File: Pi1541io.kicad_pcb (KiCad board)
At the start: 2 copper layers, 65 x 56 mm, 56 parts, among them J1 IEC1, J10 SDA, J11 SCL, J12 I2C, J13 SDA, J14 SDA, J15 SDA, J2 IEC2, J3 IEC3, J4 ExtSpkr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

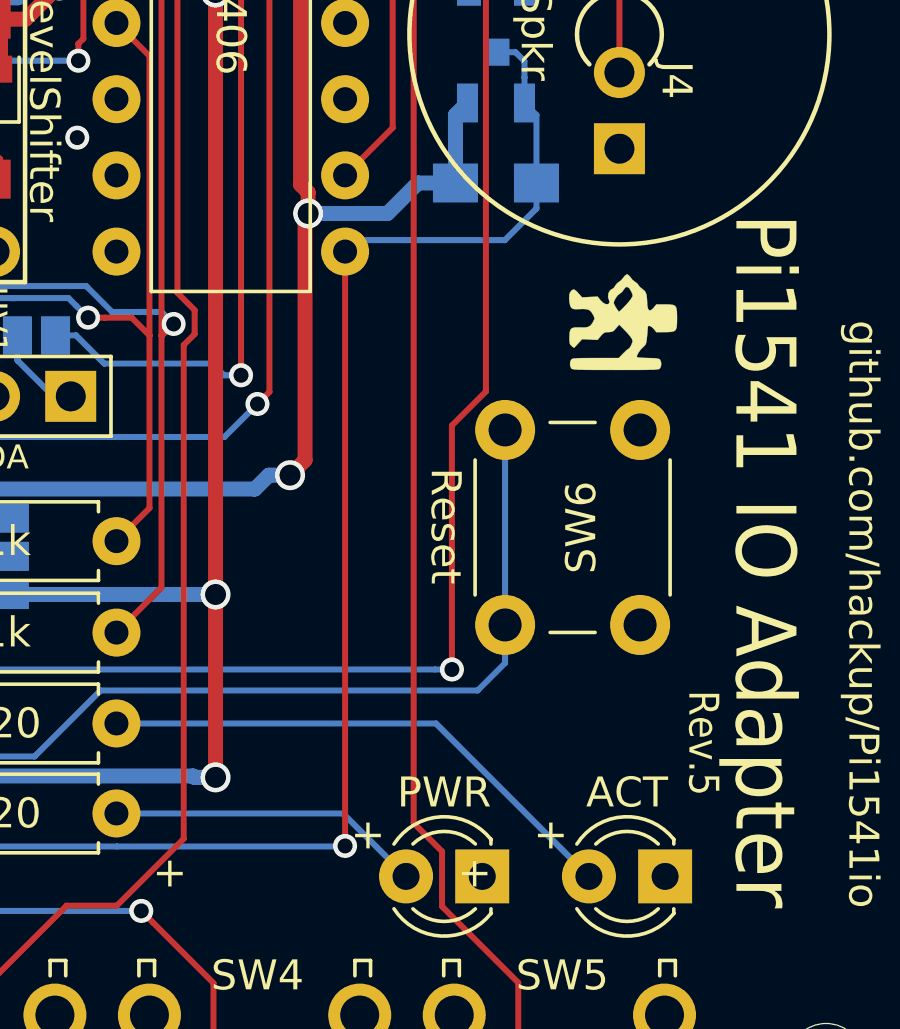
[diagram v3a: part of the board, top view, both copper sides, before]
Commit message: Added an additional solder bridge that is now needed to connect the SRQ line from the bus. This closes #1.
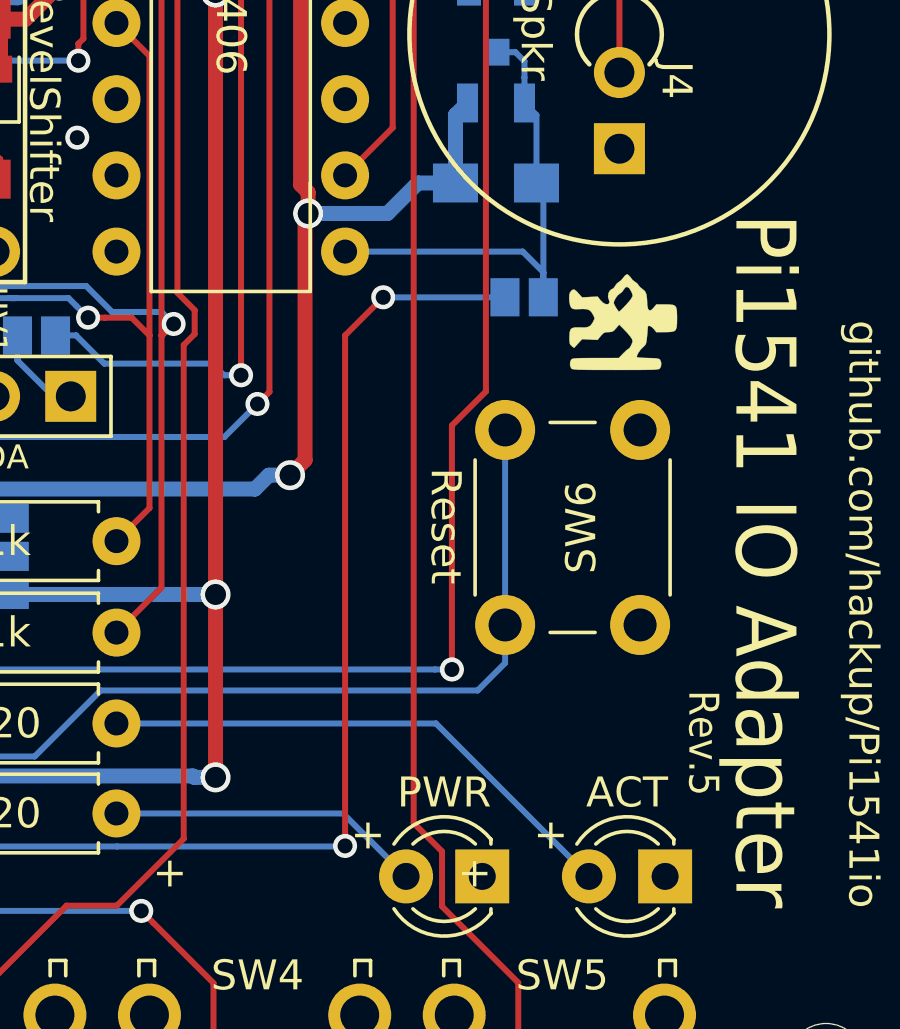
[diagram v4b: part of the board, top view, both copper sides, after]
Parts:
- added J16: GS2, Connectors:GS2, B.Cu at (157.6, 86.2)
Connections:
- Q5 pad 3: SRQ -> Net-(J16-Pad2)
- R13 pad 2: SRQ -> Net-(J16-Pad2)
- R15 pad 2: SRQ -> Net-(J16-Pad2)
- U2 pad 8: SRQ -> Net-(J16-Pad2)
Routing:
- net Net-(J16-Pad2): track 0.00 -> 16.9 mm
- net SRQ: track 89.8 -> 79.8 mm, vias 1 -> 2
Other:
- board text added: "enable"
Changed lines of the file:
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@@
   (general
     (thickness 1.6)
-    (drawings 120)
-    (tracks 610)
+    (drawings 121)
+    (tracks 613)
     (zones 0)
-    (modules 56)
-    (nets 41)
+    (modules 57)
+    (nets 42)
   )
   (page A4)
@@
   (net 39 "Net-(J12-Pad4)")
   (net 40 "Net-(J13-Pad1)")
+  (net 41 "Net-(J16-Pad2)")
   (net_class Default "This is the default net class."
     (clearance 0.2)
@@
     (add_net "Net-(J10-Pad2)")
     (add_net "Net-(J11-Pad2)")
+    (add_net "Net-(J16-Pad2)")
     (add_net "Net-(J4-Pad1)")
     (add_net RESET)
@@
       (net 20 DATA_BD))
     (pad 8 thru_hole oval (at 7.62 15.24) (size 1.6 1.6) (drill 0.8) (layers *.Cu *.Mask)
-      (net 17 SRQ))
+      (net 41 "Net-(J16-Pad2)"))
     (pad 2 thru_hole oval (at 0 2.54) (size 1.6 1.6) (drill 0.8) (layers *.Cu *.Mask)
       (net 14 DATA))
@@
       (net 30 SRQ_3V))
     (pad 3 smd rect (at 1 0 270) (size 0.9 0.8) (layers B.Cu B.Paste B.Mask)
-      (net 17 SRQ))
+      (net 41 "Net-(J16-Pad2)"))
     (model ${KISYS3DMOD}/TO_SOT_Packages_SMD.3dshapes/SOT-23.wrl
       (at (xyz 0 0 0))
@@
     )
     (pad 2 smd rect (at 0.95 0) (size 0.7 1.3) (layers B.Cu B.Paste B.Mask)
-      (net 17 SRQ))
+      (net 41 "Net-(J16-Pad2)"))
     (pad 1 smd rect (at -0.95 0) (size 0.7 1.3) (layers B.Cu B.Paste B.Mask)
       (net 2 +5V))
@@
       (net 2 +5V))
     (pad 2 smd rect (at 1.35 0) (size 1.5 1.3) (layers B.Cu B.Paste B.Mask)
-      (net 17 SRQ))
+      (net 41 "Net-(J16-Pad2)"))
     (model ${KISYS3DMOD}/Resistors_SMD.3dshapes/R_0805.wrl
       (at (xyz 0 0 0))
@@
     (pad "" np_thru_hole oval (at 0 0) (size 3.2 1.5) (drill oval 2.7 1.1) (layers *.Cu *.Mask))
   )
+  (module Connectors:GS2 (layer B.Cu)
+    (at 157.582 86.246 270)
+    (descr "2-pin solder bridge")
+    (tags "solder bridge")
+    (attr smd)
+    (fp_text reference J16 (at 0 2.54) (layer B.SilkS)
+      (effects (font (size 0.8 0.8) (thickness 0.12)) (justify mirror))
+    )
+    (fp_text value GS2 (at -1.8 0 180) (layer B.Fab)
+      (effects (font (size 1 1) (thickness 0.15)) (justify mirror))
+    )
+    (fp_line (start 1.1 1.45) (end 1.1 -1.5) (layer B.CrtYd) (width 0.05))
+    (fp_line (start 1.1 -1.5) (end -1.1 -1.5) (layer B.CrtYd) (width 0.05))
+    (fp_line (start -1.1 -1.5) (end -1.1 1.45) (layer B.CrtYd) (width 0.05))
+    (fp_line (start -1.1 1.45) (end 1.1 1.45) (layer B.CrtYd) (width 0.05))
+    (fp_line (start -0.89 1.27) (end -0.89 -1.27) (layer B.SilkS) (width 0.12))
+    (fp_line (start 0.89 -1.27) (end 0.89 1.27) (layer B.SilkS) (width 0.12))
+    (fp_line (start 0.89 -1.27) (end -0.89 -1.27) (layer B.SilkS) (width 0.12))
+    (fp_line (start -0.89 1.27) (end 0.89 1.27) (layer B.SilkS) (width 0.12))
+    (pad 1 smd rect (at 0 0.64 270) (size 1.27 0.97) (layers B.Cu B.Paste B.Mask)
+      (net 17 SRQ))
+    (pad 2 smd rect (at 0 -0.64 270) (size 1.27 0.97) (layers B.Cu B.Paste B.Mask)
+      (net 41 "Net-(J16-Pad2)"))
+  )
+  (gr_text enable (at 156.947 87.643) (layer B.SilkS)
+    (effects (font (size 0.8 0.8) (thickness 0.12)) (justify mirror))
+  )
   (gr_text + (at 158.471 104.153) (layer F.SilkS)
     (effects (font (size 1 1) (thickness 0.2)))
@@
     (effects (font (size 0.8 0.8) (thickness 0.15)))
   )
-  (gr_text "SRQ\nreserved" (at 159.487 83.706) (layer B.SilkS)
+  (gr_text "SRQ\nreserved" (at 159.487 87.262) (layer B.SilkS)
     (effects (font (size 1 1) (thickness 0.15)) (justify right mirror))
   )
-  (gr_line (start 159.487 67.958) (end 159.487 84.976) (layer B.SilkS) (width 0.1))
+  (gr_line (start 159.487 67.958) (end 159.487 88.786) (layer B.SilkS) (width 0.1))
   (gr_line (start 153.645 67.958) (end 159.487 67.958) (layer B.SilkS) (width 0.1))
-  (gr_line (start 153.645 84.976) (end 153.645 67.958) (layer B.SilkS) (width 0.1))
-  (gr_line (start 159.487 84.976) (end 153.645 84.976) (layer B.SilkS) (width 0.1))
+  (gr_line (start 153.645 88.786) (end 153.645 67.958) (layer B.SilkS) (width 0.1))
+  (gr_line (start 159.487 88.786) (end 153.645 88.786) (layer B.SilkS) (width 0.1))
   (gr_line (start 135.103 70.625) (end 135.103 70.371) (layer B.SilkS) (width 0.1))
   (gr_line (start 135.103 70.879) (end 135.103 71.133) (layer B.SilkS) (width 0.1))
@@
   (segment (start 117.577 86.228345) (end 119.127001 87.778346) (width 0.2) (layer F.Cu) (net 17))
   (segment (start 117.577 84.602) (end 117.577 86.228345) (width 0.2) (layer F.Cu) (net 17) (status 10))
-  (segment (start 157.9922 80.169) (end 157.5922 79.769) (width 0.2) (layer B.Cu) (net 17))
-  (segment (start 157.9922 82.436) (end 157.9922 80.169) (width 0.2) (layer B.Cu) (net 17))
-  (segment (start 157.5922 78.919) (end 157.5922 79.769) (width 0.2) (layer B.Cu) (net 17))
-  (segment (start 157.5922 78.3758) (end 157.5922 78.919) (width 0.2) (layer B.Cu) (net 17))
-  (segment (start 157.293 78.0766) (end 157.5922 78.3758) (width 0.2) (layer B.Cu) (net 17))
-  (segment (start 156.693 78.0766) (end 157.293 78.0766) (width 0.2) (layer B.Cu) (net 17))
-  (segment (start 157.9922 83.286) (end 157.9922 82.436) (width 0.2) (layer B.Cu) (net 17))
-  (segment (start 156.9372 84.341) (end 157.9922 83.286) (width 0.2) (layer B.Cu) (net 17))
-  (segment (start 153.645 84.341) (end 156.9372 84.341) (width 0.2) (layer B.Cu) (net 17))
+  (segment (start 157.9922 80.169) (end 157.5922 79.769) (width 0.2) (layer B.Cu) (net 41))
+  (segment (start 157.9922 82.436) (end 157.9922 80.169) (width 0.2) (layer B.Cu) (net 41))
+  (segment (start 157.5922 78.919) (end 157.5922 79.769) (width 0.2) (layer B.Cu) (net 41))
+  (segment (start 157.5922 78.3758) (end 157.5922 78.919) (width 0.2) (layer B.Cu) (net 41))
+  (segment (start 157.293 78.0766) (end 157.5922 78.3758) (width 0.2) (layer B.Cu) (net 41))
+  (segment (start 156.693 78.0766) (end 157.293 78.0766) (width 0.2) (layer B.Cu) (net 41))
   (segment (start 119.203345 104.922) (end 117.577 104.922) (width 0.2) (layer B.Cu) (net 17))
   (segment (start 125.029 104.922) (end 119.203345 104.922) (width 0.2) (layer B.Cu) (net 17))
   (segment (start 126.179 103.772) (end 125.029 104.922) (width 0.2) (layer B.Cu) (net 17))
   (segment (start 127.229 103.772) (end 126.179 103.772) (width 0.2) (layer B.Cu) (net 17))
-  (segment (start 128.279 103.772) (end 127.229 103.772) (width 0.2) (layer B.Cu) (net 17))
-  (segment (start 129.059001 104.552001) (end 128.279 103.772) (width 0.2) (layer B.Cu) (net 17))
-  (segment (start 144.011001 104.552001) (end 129.059001 104.552001) (width 0.2) (layer B.Cu) (net 17))
-  (segment (start 151.994 84.341) (end 151.613 84.722) (width 0.2) (layer B.Cu) (net 17))
-  (segment (start 153.645 84.341) (end 151.994 84.341) (width 0.2) (layer B.Cu) (net 17))
   (via (at 151.613 104.534) (size 0.8) (drill 0.5) (layers F.Cu B.Cu) (net 17))
-  (segment (start 144.011001 104.552001) (end 151.594999 104.552001) (width 0.2) (layer B.Cu) (net 17))
+  (segment (start 151.613 87.516) (end 152.883 86.246) (width 0.2) (layer F.Cu) (net 17))
+  (segment (start 151.613 104.534) (end 151.613 87.516) (width 0.2) (layer F.Cu) (net 17))
+  (via (at 152.883 86.246) (size 0.8) (drill 0.5) (layers F.Cu B.Cu) (net 17))
   (segment (start 151.594999 104.552001) (end 151.613 104.534) (width 0.2) (layer B.Cu) (net 17))
-  (segment (start 151.613 104.534) (end 151.613 84.722) (width 0.2) (layer F.Cu) (net 17))
+  (segment (start 144.011001 104.552001) (end 151.594999 104.552001) (width 0.2) (layer B.Cu) (net 17))
+  (segment (start 144.011001 104.552001) (end 129.059001 104.552001) (width 0.2) (layer B.Cu) (net 17))
+  (segment (start 129.059001 104.552001) (end 128.279 103.772) (width 0.2) (layer B.Cu) (net 17))
+  (segment (start 128.279 103.772) (end 127.229 103.772) (width 0.2) (layer B.Cu) (net 17))
+  (segment (start 152.883 86.246) (end 156.942 86.246) (width 0.2) (layer B.Cu) (net 17))
   (via (at 161.011 67.704) (size 0.8) (drill 0.5) (layers F.Cu B.Cu) (net 18))
   (segment (start 161.086999 62.281999) (end 160.237 61.432) (width 0.2) (layer F.Cu) (net 18))
@@
   (segment (start 131.547 96.779) (end 133.440001 98.672001) (width 0.5) (layer B.Cu) (net 40))
   (segment (start 131.547 95.644) (end 131.547 96.779) (width 0.5) (layer B.Cu) (net 40))
+  (segment (start 158.222 82.6658) (end 157.9922 82.436) (width 0.2) (layer B.Cu) (net 41))
+  (segment (start 158.222 86.246) (end 158.222 82.6658) (width 0.2) (layer B.Cu) (net 41))
+  (segment (start 158.222 85.411) (end 158.222 86.246) (width 0.2) (layer B.Cu) (net 41))
+  (segment (start 157.533 84.722) (end 158.222 85.411) (width 0.2) (layer B.Cu) (net 41))
+  (segment (start 151.613 84.722) (end 157.533 84.722) (width 0.2) (layer B.Cu) (net 41))
   (zone (net 3) (net_name GND) (layer F.Cu) (hatch edge 0.508)
     (connect_pads (clearance 0.4))

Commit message: Optimized silk screen.
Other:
- board text added: "SRQ"
- board text removed: "SRQ reserved"
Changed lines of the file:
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@@
       (net 41 "Net-(J16-Pad2)"))
   )
-  (gr_text enable (at 156.947 87.643) (layer B.SilkS)
+  (gr_text enable (at 156.947 87.77) (layer B.SilkS)
     (effects (font (size 0.8 0.8) (thickness 0.12)) (justify mirror))
   )
@@
     (effects (font (size 0.8 0.8) (thickness 0.15)))
   )
-  (gr_text "SRQ\nreserved" (at 159.487 87.262) (layer B.SilkS)
+  (gr_text SRQ (at 159.614 87.897) (layer B.SilkS)
     (effects (font (size 1 1) (thickness 0.15)) (justify right mirror))
   )

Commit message: Fine tuning.
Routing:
- net GND: vias 13 -> 15
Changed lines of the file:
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@@
     (thickness 1.6)
     (drawings 121)
-    (tracks 613)
+    (tracks 615)
     (zones 0)
     (modules 57)
@@
     (38 B.Mask user)
     (39 F.Mask user)
-    (40 Dwgs.User user hide)
+    (40 Dwgs.User user)
     (41 Cmts.User user)
     (42 Eco1.User user)
@@
     (47 F.CrtYd user)
     (48 B.Fab user)
-    (49 F.Fab user hide)
+    (49 F.Fab user)
   )
   (setup
@@
       (net 41 "Net-(J16-Pad2)"))
   )
+  (gr_line (start 142.844 88.5) (end 142.847 85.865) (layer B.SilkS) (width 0.1))
   (gr_text enable (at 156.947 87.77) (layer B.SilkS)
     (effects (font (size 0.8 0.8) (thickness 0.12)) (justify mirror))
@@
     (effects (font (size 1 1) (thickness 0.22)))
   )
-  (gr_text + (at 145.771 105.423) (layer F.SilkS)
-    (effects (font (size 1 1) (thickness 0.22)))
-  )
   (gr_text "I2C\nConfig" (at 142.723 101.74) (layer B.SilkS)
     (effects (font (size 0.8 0.8) (thickness 0.2)) (justify left mirror))
   )
   (gr_line (start 128.372 85.865) (end 142.85 85.865) (layer B.SilkS) (width 0.1))
-  (gr_line (start 142.847 103.392) (end 142.85 85.865) (layer B.SilkS) (width 0.1))
+  (gr_line (start 142.847 103.392) (end 142.85 90.5) (layer B.SilkS) (width 0.1))
   (gr_line (start 128.372 103.391) (end 135.1 103.391) (layer B.SilkS) (width 0.1))
   (gr_line (start 128.372 85.865) (end 128.372 103.391) (layer B.SilkS) (width 0.1))
@@
   (gr_line (start 140.691 86.246) (end 135.611 86.246) (layer B.SilkS) (width 0.1))
   (gr_line (start 140.691 86.627) (end 140.691 86.246) (layer B.SilkS) (width 0.1))
-  (gr_text SDA (at 139.929 91.58) (layer F.SilkS)
+  (gr_text SDA (at 142.469 91.58) (layer F.SilkS)
     (effects (font (size 0.8 0.8) (thickness 0.15)))
   )
-  (gr_text SCL (at 137.389 91.58) (layer F.SilkS)
+  (gr_text SCL (at 139.929 91.58) (layer F.SilkS)
     (effects (font (size 0.8 0.8) (thickness 0.15)))
   )
-  (gr_text Power (at 133.579 91.58) (layer F.SilkS)
+  (gr_text Power (at 136.119 91.58) (layer F.SilkS)
     (effects (font (size 0.8 0.8) (thickness 0.15)))
   )
@@
   (segment (start 147.532998 70.752) (end 147.540999 70.743999) (width 0.5) (layer B.Cu) (net 3))
   (segment (start 147.041 70.752) (end 147.532998 70.752) (width 0.5) (layer B.Cu) (net 3))
+  (via (at 152.797 95.552) (size 0.8) (drill 0.5) (layers F.Cu B.Cu) (net 3))
+  (via (at 117.497 100.702) (size 0.8) (drill 0.5) (layers F.Cu B.Cu) (net 3))
   (segment (start 150.926999 64.821999) (end 150.077 63.972) (width 0.2) (layer F.Cu) (net 4))
   (segment (start 154.845001 106.550003) (end 154.845001 104.716003) (width 0.2) (layer F.Cu) (net 4))
@@
   (segment (start 117.577 86.228345) (end 119.127001 87.778346) (width 0.2) (layer F.Cu) (net 17))
   (segment (start 117.577 84.602) (end 117.577 86.228345) (width 0.2) (layer F.Cu) (net 17) (status 10))
-  (segment (start 157.9922 80.169) (end 157.5922 79.769) (width 0.2) (layer B.Cu) (net 41))
-  (segment (start 157.9922 82.436) (end 157.9922 80.169) (width 0.2) (layer B.Cu) (net 41))
-  (segment (start 157.5922 78.919) (end 157.5922 79.769) (width 0.2) (layer B.Cu) (net 41))
-  (segment (start 157.5922 78.3758) (end 157.5922 78.919) (width 0.2) (layer B.Cu) (net 41))
-  (segment (start 157.293 78.0766) (end 157.5922 78.3758) (width 0.2) (layer B.Cu) (net 41))
-  (segment (start 156.693 78.0766) (end 157.293 78.0766) (width 0.2) (layer B.Cu) (net 41))
   (segment (start 119.203345 104.922) (end 117.577 104.922) (width 0.2) (layer B.Cu) (net 17))
   (segment (start 125.029 104.922) (end 119.203345 104.922) (width 0.2) (layer B.Cu) (net 17))
@@
   (segment (start 131.547 96.779) (end 133.440001 98.672001) (width 0.5) (layer B.Cu) (net 40))
   (segment (start 131.547 95.644) (end 131.547 96.779) (width 0.5) (layer B.Cu) (net 40))
+  (segment (start 157.9922 80.169) (end 157.5922 79.769) (width 0.2) (layer B.Cu) (net 41))
+  (segment (start 157.9922 82.436) (end 157.9922 80.169) (width 0.2) (layer B.Cu) (net 41))
+  (segment (start 157.5922 78.919) (end 157.5922 79.769) (width 0.2) (layer B.Cu) (net 41))
+  (segment (start 157.5922 78.3758) (end 157.5922 78.919) (width 0.2) (layer B.Cu) (net 41))
+  (segment (start 157.293 78.0766) (end 157.5922 78.3758) (width 0.2) (layer B.Cu) (net 41))
+  (segment (start 156.693 78.0766) (end 157.293 78.0766) (width 0.2) (layer B.Cu) (net 41))
   (segment (start 158.222 82.6658) (end 157.9922 82.436) (width 0.2) (layer B.Cu) (net 41))
   (segment (start 158.222 86.246) (end 158.222 82.6658) (width 0.2) (layer B.Cu) (net 41))
